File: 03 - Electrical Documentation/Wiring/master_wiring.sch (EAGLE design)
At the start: 62 parts

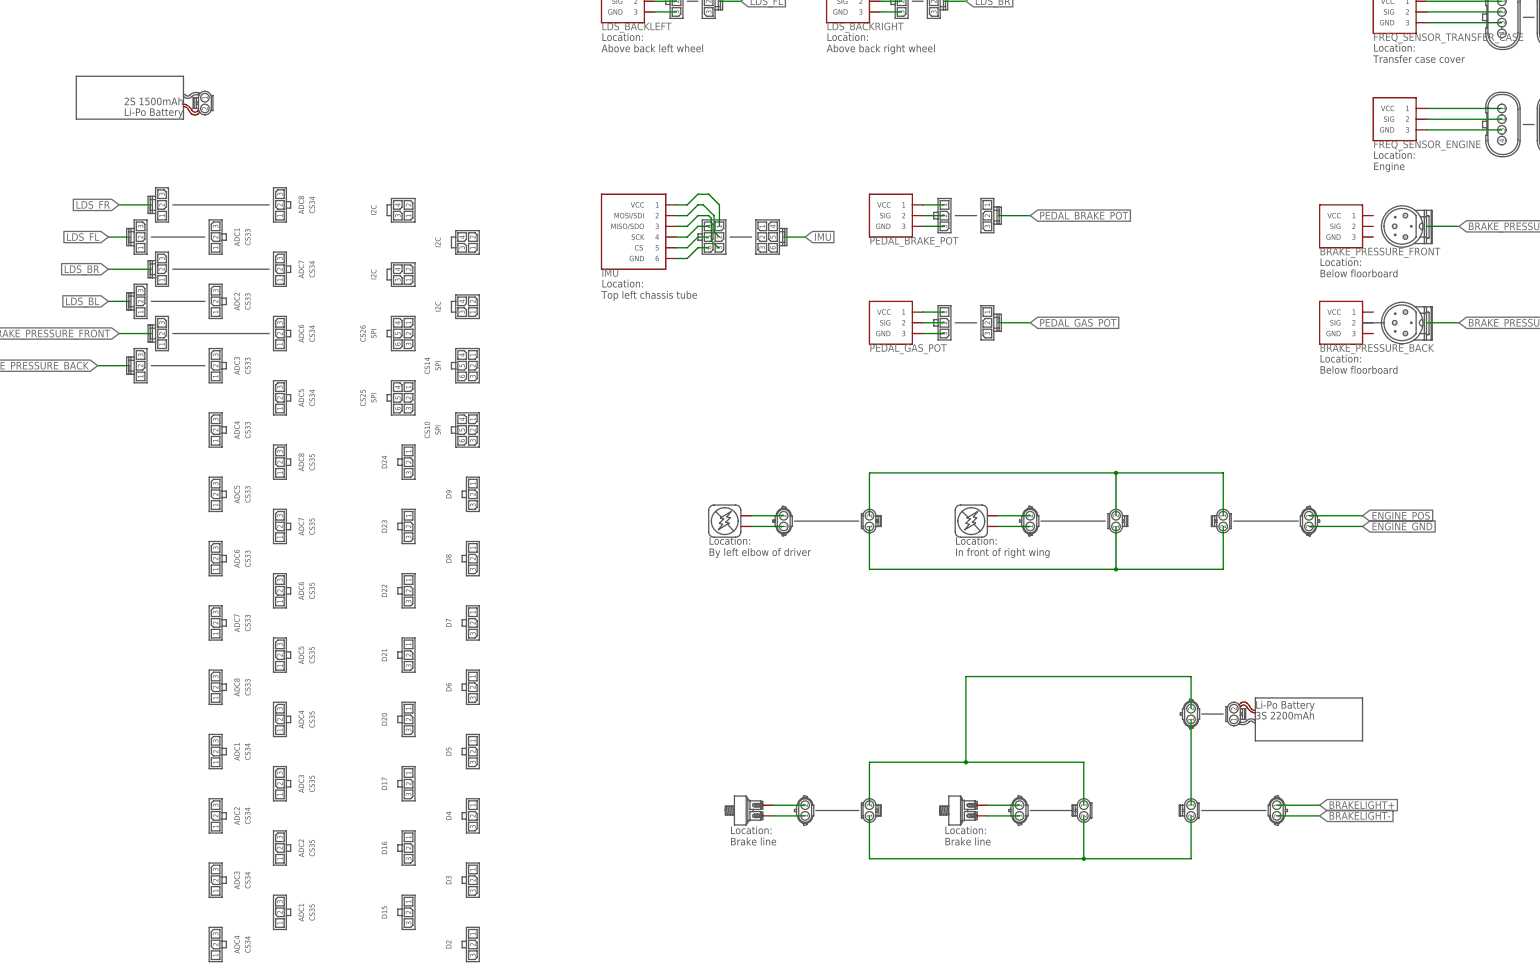
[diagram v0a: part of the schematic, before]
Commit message: Added documentation worked on during summer
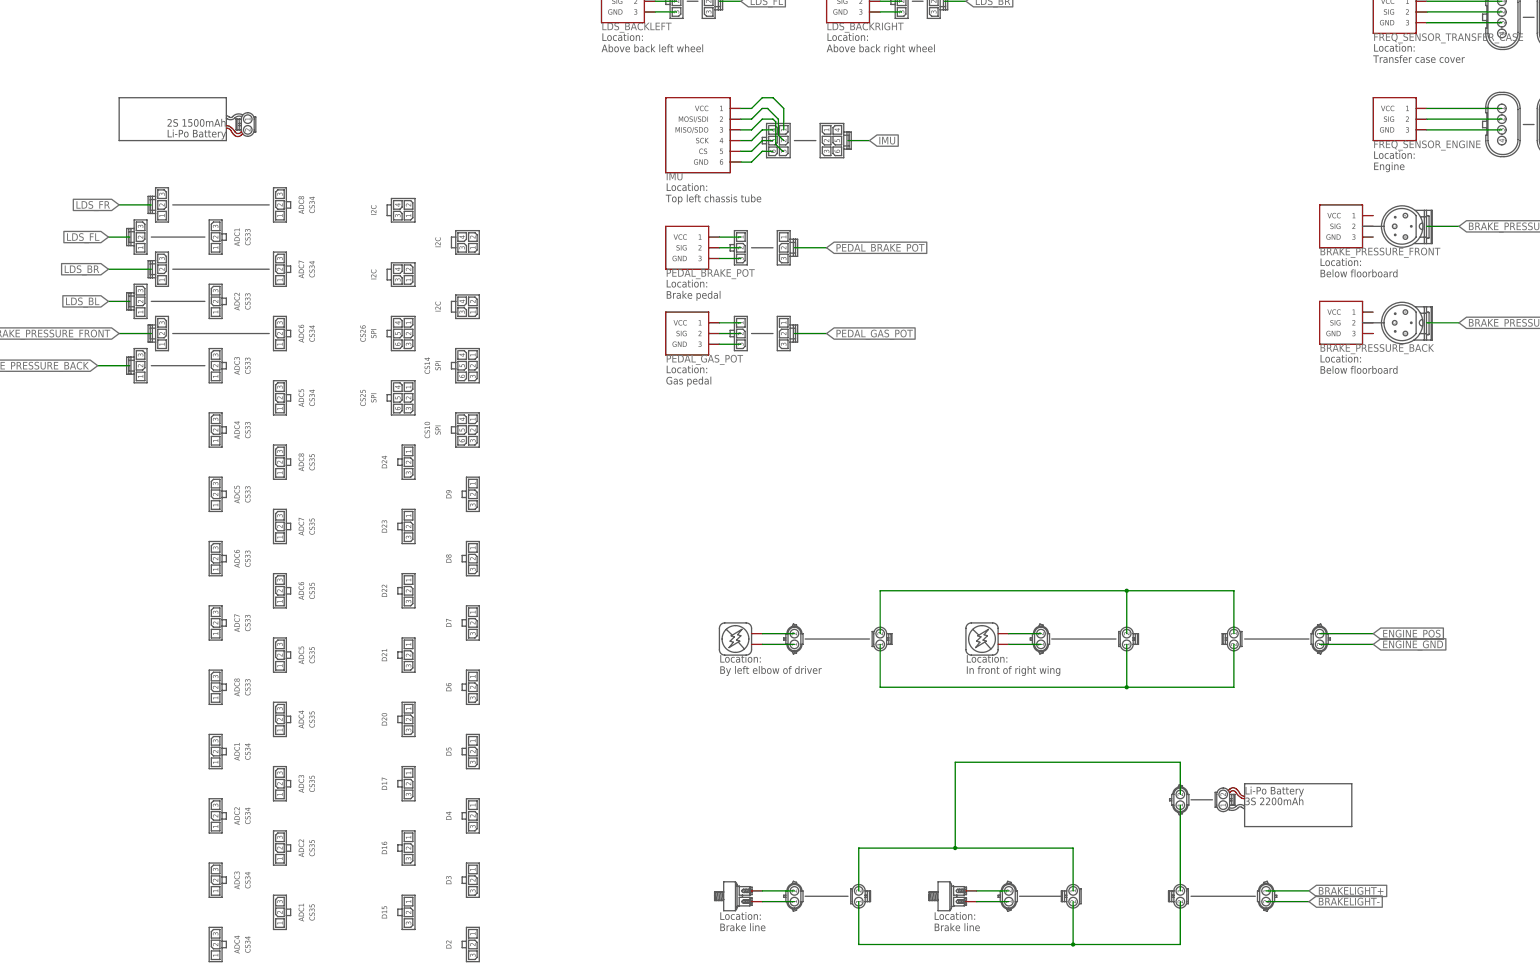
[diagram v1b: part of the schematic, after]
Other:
- note added: "Location: Brake pedal"
- note added: "Location: Gas pedal"
- moved on the sheet: IMU, PEDAL_BRAKE_POT, PEDAL_GAS_POT
